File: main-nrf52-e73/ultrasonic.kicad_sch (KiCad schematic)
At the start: 14 parts, among them U10 TUSS4440

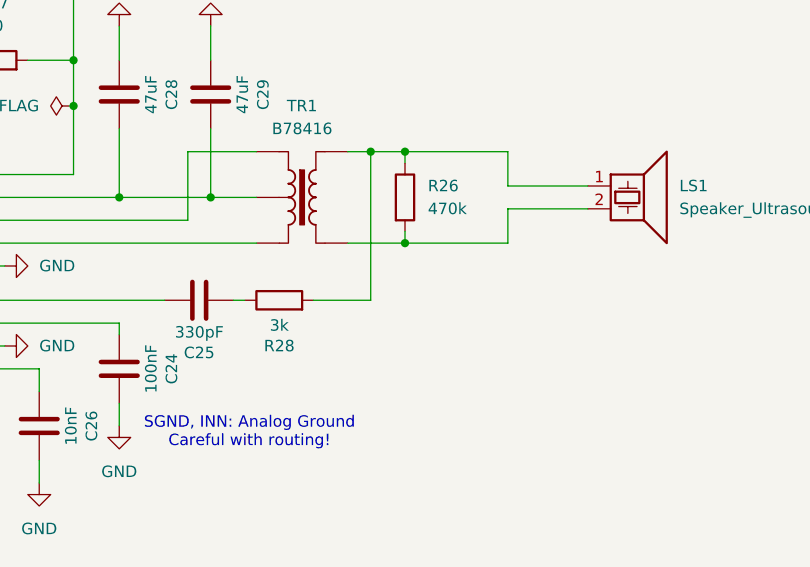
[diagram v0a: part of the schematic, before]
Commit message: Finished first prototype of nRF52 powered main PCB.
Using Ebyte E73 module for the nRF chip.
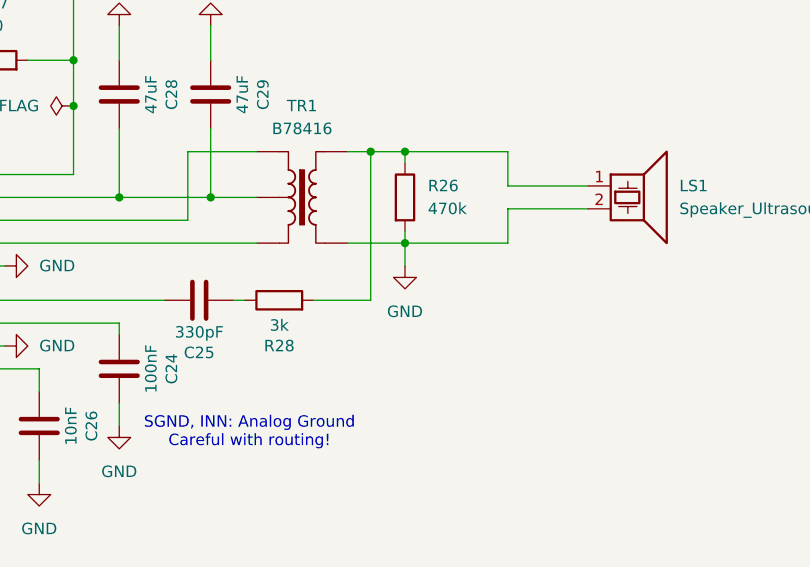
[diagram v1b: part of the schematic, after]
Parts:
- C24: footprint Capacitor_SMD:C_0805_2012Metric -> Capacitor_SMD:C_0603_1608Metric; LCSC (none) -> C14663
- C25: LCSC (none) -> C1664
- C26: LCSC (none) -> C57112
- C27, C28, C29: LCSC (none) -> C96123
- C30: LCSC (none) -> C15850
- R26: LCSC (none) -> C23178
- R27: LCSC (none) -> C22859
- R28: LCSC (none) -> C4211
- R29: LCSC (none) -> C22775
- U10: LCSC (none) -> C1855778
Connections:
- net GND: now also LS1.2, R26.2, TR1.4
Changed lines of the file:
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@@
+	(wire
+		(pts
+			(xy 199.39 74.93) (xy 199.39 77.47)
+		)
+		(stroke
+			(width 0)
+			(type default)
+		)
+	)
 	(wire
 		(pts
@@
 			)
 		)
+		(property "LCSC" "C96123"
+			(at 177.8 58.42 0)
+			(effects
+				(font
+					(size 1.27 1.27)
+				)
+				(hide yes)
+			)
+		)
 		(pin "1"
 		)
@@
 			)
 		)
+		(property "LCSC" "C96123"
+			(at 162.56 40.64 0)
+			(effects
+				(font
+					(size 1.27 1.27)
+				)
+				(hide yes)
+			)
+		)
 		(pin "1"
 		)
@@
 			)
 		)
+		(property "LCSC" "C1855778"
+			(at 140.97 78.74 0)
+			(effects
+				(font
+					(size 1.27 1.27)
+				)
+				(hide yes)
+			)
+		)
 		(pin "17"
 		)
@@
 			)
 		)
+		(property "LCSC" "C15850"
+			(at 123.19 63.5 0)
+			(effects
+				(font
+					(size 1.27 1.27)
+				)
+				(hide yes)
+			)
+		)
 		(pin "1"
 		)
@@
 			)
 		)
+		(property "LCSC" ""
+			(at 224.79 68.58 0)
+			(effects
+				(font
+					(size 1.27 1.27)
+				)
+				(hide yes)
+			)
+		)
 		(pin "1"
 		)
@@
 			)
 		)
+		(property "LCSC" "C4211"
+			(at 185.42 81.28 0)
+			(effects
+				(font
+					(size 1.27 1.27)
+				)
+				(hide yes)
+			)
+		)
 		(pin "2"
 		)
@@
 			)
 		)
+		(property "LCSC" "C22859"
+			(at 153.67 54.61 0)
+			(effects
+				(font
+					(size 1.27 1.27)
+				)
+				(hide yes)
+			)
+		)
 		(pin "2"
 		)
@@
 			)
 		)
+		(property "LCSC" "C96123"
+			(at 167.64 58.42 0)
+			(effects
+				(font
+					(size 1.27 1.27)
+				)
+				(hide yes)
+			)
+		)
 		(pin "1"
 		)
@@
 			)
 		)
+		(property "LCSC" "C22775"
+			(at 118.11 86.36 0)
+			(effects
+				(font
+					(size 1.27 1.27)
+				)
+				(hide yes)
+			)
+		)
 		(pin "2"
 		)
@@
 			)
 		)
+		(property "LCSC" "C57112"
+			(at 158.75 95.25 0)
+			(effects
+				(font
+					(size 1.27 1.27)
+				)
+				(hide yes)
+			)
+		)
 		(pin "1"
 		)
@@
 				(path "/8640b7d9-2e5e-48c6-a85a-cc24a7b66a1a/f500bce4-2db0-42cc-af0b-38b381f78534"
 					(reference "C26")
+					(unit 1)
+				)
+			)
+		)
+	)
+	(symbol
+		(lib_id "power:GND")
+		(at 199.39 77.47 0)
+		(unit 1)
+		(exclude_from_sim no)
+		(in_bom yes)
+		(on_board yes)
+		(dnp no)
+		(fields_autoplaced yes)
+		(property "Reference" "#PWR027"
+			(at 199.39 83.82 0)
+			(effects
+				(font
+					(size 1.27 1.27)
+				)
+				(hide yes)
+			)
+		)
+		(property "Value" "GND"
+			(at 199.39 82.55 0)
+			(effects
+				(font
+					(size 1.27 1.27)
+				)
+			)
+		)
+		(property "Footprint" ""
+			(at 199.39 77.47 0)
+			(effects
+				(font
+					(size 1.27 1.27)
+				)
+				(hide yes)
+			)
+		)
+		(property "Datasheet" ""
+			(at 199.39 77.47 0)
+			(effects
+				(font
+					(size 1.27 1.27)
+				)
+				(hide yes)
+			)
+		)
+		(property "Description" "Power symbol creates a global label with name \"GND\" , ground"
+			(at 199.39 77.47 0)
+			(effects
+				(font
+					(size 1.27 1.27)
+				)
+				(hide yes)
+			)
+		)
+		(pin "1"
+		)
+		(instances
+			(project "main-nrf52-e73"
+				(path "/8640b7d9-2e5e-48c6-a85a-cc24a7b66a1a/f500bce4-2db0-42cc-af0b-38b381f78534"
+					(reference "#PWR027")
 					(unit 1)
 				)
@@
 			)
 		)
+		(property "LCSC" "C23178"
+			(at 199.39 69.85 0)
+			(effects
+				(font
+					(size 1.27 1.27)
+				)
+				(hide yes)
+			)
+		)
 		(pin "2"
 		)
@@
 			)
 		)
+		(property "LCSC" "C1664"
+			(at 176.53 81.28 0)
+			(effects
+				(font
+					(size 1.27 1.27)
+				)
+				(hide yes)
+			)
+		)
 		(pin "1"
 		)
@@
 			)
 		)
-		(property "Footprint" "Capacitor_SMD:C_0805_2012Metric"
+		(property "Footprint" "Capacitor_SMD:C_0603_1608Metric"
 			(at 168.6052 92.71 0)
 			(effects
@@
 			)
 		)
+		(property "LCSC" "C14663"
+			(at 167.64 88.9 0)
+			(effects
+				(font
+					(size 1.27 1.27)
+				)
+				(hide yes)
+			)
+		)
 		(pin "1"
 		)
@@
 			(at 187.96 69.85 0)
 			(effects
+				(font
+					(size 1.27 1.27)
+				)
+				(hide yes)
+			)
+		)
+		(property "LCSC" ""
+			(at 187.96 69.85 0)
+			(effects
